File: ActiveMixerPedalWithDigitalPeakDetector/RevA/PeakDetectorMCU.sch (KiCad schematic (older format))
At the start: 22 parts, among them J7 Conn_01x05, U11 STM32F051K8Tx

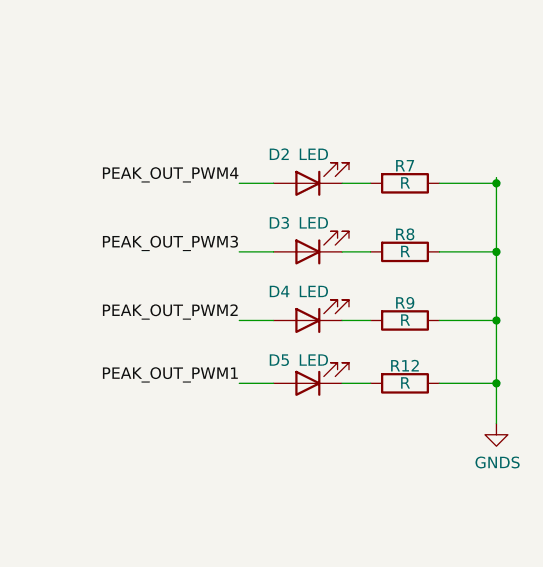
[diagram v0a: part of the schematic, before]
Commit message: hardware update
set led resistor value
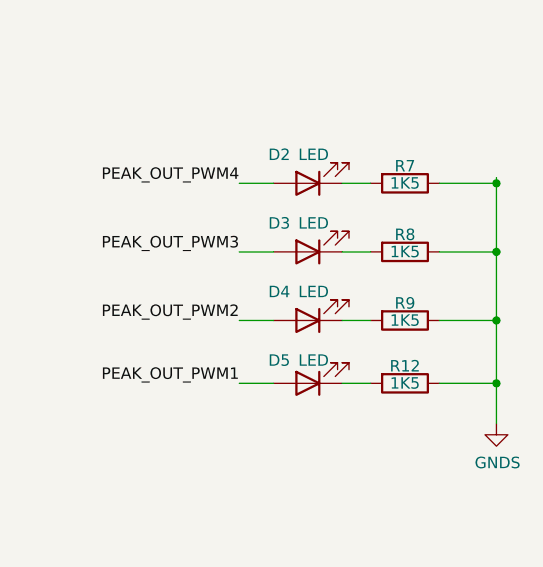
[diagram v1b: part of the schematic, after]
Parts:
- R12, R7, R8, R9: value R -> 1K5
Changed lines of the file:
@@
 P 10025 3175
 F 0 "R12" V 9950 3175 50  0000 C CNN
-F 1 "R" V 10025 3175 50  0000 C CNN
+F 1 "1K5" V 10025 3175 50  0000 C CNN
 F 2 "Resistor_SMD:R_0805_2012Metric_Pad1.15x1.40mm_HandSolder" V 9955 3175 50  0001 C CNN
 F 3 "~" H 10025 3175 50  0001 C CNN
@@
 P 10025 2900
 F 0 "R9" V 9950 2900 50  0000 C CNN
-F 1 "R" V 10025 2900 50  0000 C CNN
+F 1 "1K5" V 10025 2900 50  0000 C CNN
 F 2 "Resistor_SMD:R_0805_2012Metric_Pad1.15x1.40mm_HandSolder" V 9955 2900 50  0001 C CNN
 F 3 "~" H 10025 2900 50  0001 C CNN
@@
 P 10025 2600
 F 0 "R8" V 9950 2600 50  0000 C CNN
-F 1 "R" V 10025 2600 50  0000 C CNN
+F 1 "1K5" V 10025 2600 50  0000 C CNN
 F 2 "Resistor_SMD:R_0805_2012Metric_Pad1.15x1.40mm_HandSolder" V 9955 2600 50  0001 C CNN
 F 3 "~" H 10025 2600 50  0001 C CNN
@@
 P 10025 2300
 F 0 "R7" V 9950 2300 50  0000 C CNN
-F 1 "R" V 10025 2300 50  0000 C CNN
+F 1 "1K5" V 10025 2300 50  0000 C CNN
 F 2 "Resistor_SMD:R_0805_2012Metric_Pad1.15x1.40mm_HandSolder" V 9955 2300 50  0001 C CNN
 F 3 "~" H 10025 2300 50  0001 C CNN
